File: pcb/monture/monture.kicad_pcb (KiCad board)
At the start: 2 copper layers, 150 x 110 mm, 37 parts, among them U1 Teensy 4.1

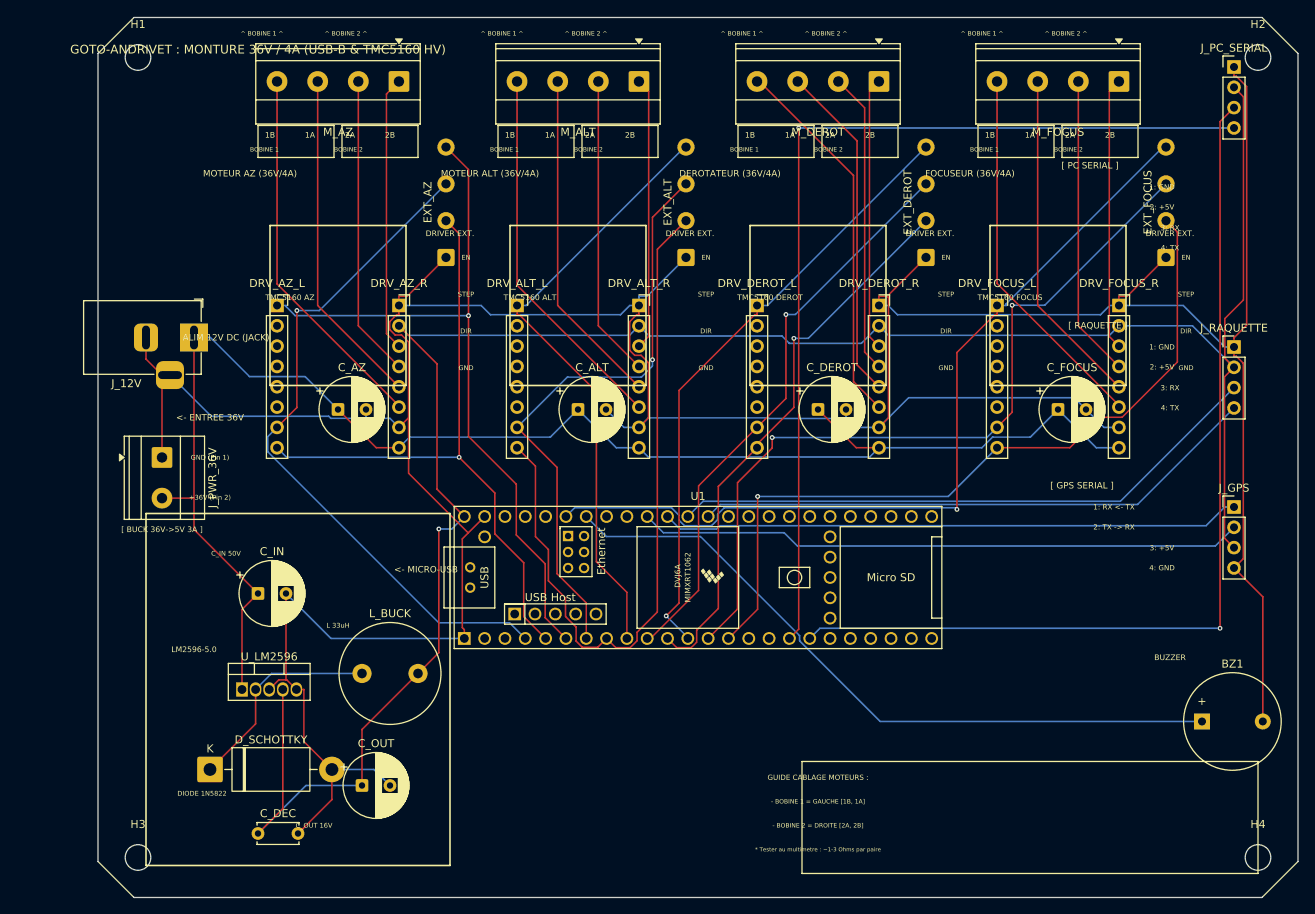
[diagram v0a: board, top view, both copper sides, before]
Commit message: PCB monture : supports StepStick, routage puissance et selecteur de drivers externes
Plan de cablage (README / fiche technique) inchange : memes broches Teensy.

PCB monture
- Supports StepStick a l'entraxe standard 12,7 mm, colonne puissance dans
  l'ordre Pololu (VMOT en face de EN) ; l'ancien brochage mettait le +36V
  sur le +5V via le module. VIO des modules en 3,3 V.
- PC SERIAL : TX6 sur la broche 24 (le PCB cablait la 26), connecteur
  sorti de la zone de vis de H2 (courtyard de H2 restaure).
- Jack 12V isole du bornier 36V par D_JACK (SB560) ; diode du buck SB560
  60V (1N5822 = 40V) ; C_IN 63V deplace hors du passage du cable USB.
- Condensateurs moteur 220uF/63V D10 au-dessus des modules (un 470uF/63V
  D8 n'existe pas et etait sous le module).
- Selecteur par axe StepStick / driver externe : DIP x4 SW_SEL,
  3 x 74HC126 (3,3V) vers les supports, 3 x 74HCT125 (5V) vers les
  pastilles DRIVER EXT. (optocoupleurs M542/DM542).
- Classe de nets "Puissance" 1,5 mm restauree (perdue en f42434d : tout
  etait route en 0,2 mm) ; re-routage Freerouting + finition du buck.
  DRC : 0 erreur, 0 non connecte.
- Serigraphie : etiquettes DRIVER EXT. en face des bons trous, reperes
  EN/VM des supports, conventions RX/TX cote Teensy.

Boitiers
- Monture : ouvertures moteurs recentrees (regression a60715d), trou USB-B
  de nouveau supprime, ouvertures micro-USB Teensy et PC SERIAL, encoche
  du jack ouverte en haut, aerations au-dessus des modules.
- Raquette : trous des boutons centres sur les poussoirs (+3,25 / -2,25).
- Assemblages FreeCAD reconstruits (les App::Part etaient vides) :
  0 interference avec base, couvercle et gabarits.

Firmware Mega : ne plus piloter LED_BUILTIN (= FOCUS_EN broche 13).

build_kicad_pcbs.py aligne sur ces corrections (classes de nets ecrites
dans le .kicad_pro).

Co-Authored-By: Claude Opus 5.5 <noreply@anthropic.com>
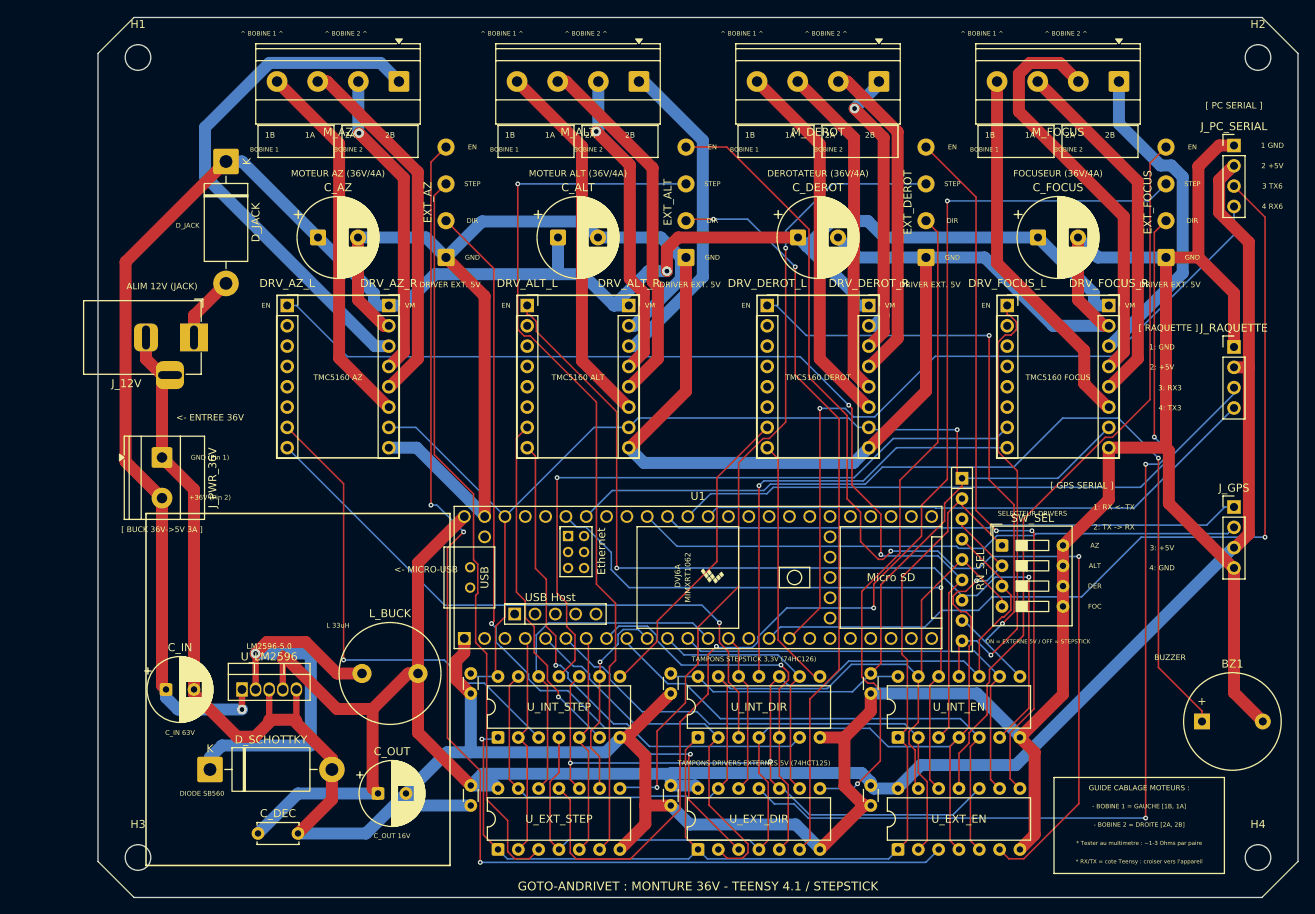
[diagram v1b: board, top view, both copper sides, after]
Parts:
- removed the C_ALT at (60.0, 49.0)
- removed the C_AZ at (30.0, 49.0)
- removed the C_DEROT at (90.0, 49.0)
- removed the C_FOCUS at (120.0, 49.0)
- added C_ALT: 220uF 63V, CP_Radial_D10.0mm_P5.00mm, F.Cu at (57.5, 27.5)
- added C_AZ: 220uF 63V, CP_Radial_D10.0mm_P5.00mm, F.Cu at (27.5, 27.5)
- added C_DEROT: 220uF 63V, CP_Radial_D10.0mm_P5.00mm, F.Cu at (87.5, 27.5)
- added C_EXT_DIR: 100nF, C_Disc_D3.0mm_W1.6mm_P2.50mm, F.Cu at (71.6, 98.5)
- added C_EXT_EN: 100nF, C_Disc_D3.0mm_W1.6mm_P2.50mm, F.Cu at (96.6, 98.5)
- added C_EXT_STEP: 100nF, C_Disc_D3.0mm_W1.6mm_P2.50mm, F.Cu at (46.6, 98.5)
- added C_FOCUS: 220uF 63V, CP_Radial_D10.0mm_P5.00mm, F.Cu at (117.5, 27.5)
- added C_INT_DIR: 100nF, C_Disc_D3.0mm_W1.6mm_P2.50mm, F.Cu at (71.6, 84.5)
- added C_INT_EN: 100nF, C_Disc_D3.0mm_W1.6mm_P2.50mm, F.Cu at (96.6, 84.5)
- added C_INT_STEP: 100nF, C_Disc_D3.0mm_W1.6mm_P2.50mm, F.Cu at (46.6, 84.5)
- added D_JACK: SB560 (60V 5A), D_DO-201AD_P15.24mm_Horizontal, F.Cu at (16.0, 18.0)
- added RN_SEL: 10k x8 (commun broche 1), R_Array_SIP9, F.Cu at (108.0, 57.6)
- added SW_SEL: DIP x4, SW_DIP_SPSTx04_Slide_9.78x12.34mm_W7.62mm_P2.54mm, F.Cu at (113.0, 66.0)
- added U_EXT_DIR: 74HCT125, DIP-14_W7.62mm, F.Cu at (75.0, 104.0)
- added U_EXT_EN: 74HCT125, DIP-14_W7.62mm, F.Cu at (100.0, 104.0)
- added U_EXT_STEP: 74HCT125, DIP-14_W7.62mm, F.Cu at (50.0, 104.0)
- added U_INT_DIR: 74HC126, DIP-14_W7.62mm, F.Cu at (75.0, 90.0)
- added U_INT_EN: 74HC126, DIP-14_W7.62mm, F.Cu at (100.0, 90.0)
- added U_INT_STEP: 74HC126, DIP-14_W7.62mm, F.Cu at (50.0, 90.0)
- C_IN: value 100uF 50V -> 100uF 63V
- D_SCHOTTKY: value 1N5822 (3A) -> SB560 (60V 5A)
- moved C_IN 16.6 mm to (8.50, 84.0)
- moved J_PC_SERIAL 9.81 mm to (142.0, 16.0)
- moved C_OUT 2.24 mm to (35.0, 97.0)
- moved DRV_ALT_R 1.27 mm to (66.3, 36.0)
- moved DRV_DEROT_L 1.27 mm to (83.7, 36.0)
- moved DRV_DEROT_R 1.27 mm to (96.3, 36.0)
- moved DRV_FOCUS_L 1.27 mm to (113.7, 36.0)
- moved DRV_FOCUS_R 1.27 mm to (126.3, 36.0)
- moved DRV_AZ_L 1.27 mm to (23.6, 36.0)
- moved DRV_ALT_L 1.27 mm to (53.6, 36.0)
- moved DRV_AZ_R 1.27 mm to (36.4, 36.0)
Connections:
- DRV_ALT_L pad 1: ALT_EN -> ALT_EN_INT
- DRV_ALT_L pad 7: ALT_STEP -> ALT_STEP_INT
- DRV_ALT_L pad 8: ALT_DIR -> ALT_DIR_INT
- DRV_ALT_R pad 1: GND -> +36V
- DRV_ALT_R pad 2: +5V -> GND
- DRV_ALT_R pad 7: GND -> +3V3
- DRV_ALT_R pad 8: +36V -> GND
- DRV_AZ_L pad 1: AZ_EN -> AZ_EN_INT
- DRV_AZ_L pad 7: AZ_STEP -> AZ_STEP_INT
- DRV_AZ_L pad 8: AZ_DIR -> AZ_DIR_INT
- DRV_AZ_R pad 1: GND -> +36V
- DRV_AZ_R pad 2: +5V -> GND
- DRV_AZ_R pad 7: GND -> +3V3
- DRV_AZ_R pad 8: +36V -> GND
- DRV_DEROT_L pad 1: DEROT_EN -> DEROT_EN_INT
- DRV_DEROT_L pad 7: DEROT_STEP -> DEROT_STEP_INT
- DRV_DEROT_L pad 8: DEROT_DIR -> DEROT_DIR_INT
- DRV_DEROT_R pad 1: GND -> +36V
- DRV_DEROT_R pad 2: +5V -> GND
- DRV_DEROT_R pad 7: GND -> +3V3
- DRV_DEROT_R pad 8: +36V -> GND
- DRV_FOCUS_L pad 1: FOCUS_EN -> FOCUS_EN_INT
- DRV_FOCUS_L pad 7: FOCUS_STEP -> FOCUS_STEP_INT
- DRV_FOCUS_L pad 8: FOCUS_DIR -> FOCUS_DIR_INT
- DRV_FOCUS_R pad 1: GND -> +36V
- DRV_FOCUS_R pad 2: +5V -> GND
- DRV_FOCUS_R pad 7: GND -> +3V3
- DRV_FOCUS_R pad 8: +36V -> GND
- EXT_ALT pad 2: ALT_DIR -> ALT_DIR_EXT
- EXT_ALT pad 3: ALT_STEP -> ALT_STEP_EXT
- EXT_ALT pad 4: ALT_EN -> ALT_EN_EXT
- EXT_AZ pad 2: AZ_DIR -> AZ_DIR_EXT
- EXT_AZ pad 3: AZ_STEP -> AZ_STEP_EXT
- EXT_AZ pad 4: AZ_EN -> AZ_EN_EXT
- EXT_DEROT pad 2: DEROT_DIR -> DEROT_DIR_EXT
- EXT_DEROT pad 3: DEROT_STEP -> DEROT_STEP_EXT
- EXT_DEROT pad 4: DEROT_EN -> DEROT_EN_EXT
- EXT_FOCUS pad 2: FOCUS_DIR -> FOCUS_DIR_EXT
- EXT_FOCUS pad 3: FOCUS_STEP -> FOCUS_STEP_EXT
- EXT_FOCUS pad 4: FOCUS_EN -> FOCUS_EN_EXT
- J_12V pad 1: +36V -> JACK_IN
- U1 pad 16: (no net) -> PC_RX
- U1 pad 18: PC_RX -> (no net)
- U1 pad 46: (no net) -> +3V3
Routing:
- net GND: track 476.6 -> 697.0 mm
- net +3V3: track 0.00 -> 193.0 mm, vias 0 -> 1
- net AZ_EN_EXT: track 0.00 -> 152.8 mm, vias 0 -> 3
- net FOCUS_STEP_EXT: track 0.00 -> 152.6 mm, vias 0 -> 3
- net SEL_AZ: track 0.00 -> 140.6 mm, vias 0 -> 1
- net ALT_EN_EXT: track 0.00 -> 135.7 mm, vias 0 -> 2
- net SEL_ALT: track 0.00 -> 132.9 mm, vias 0 -> 1
- net SEL_DEROT: track 0.00 -> 131.6 mm, vias 0 -> 2
- net FOCUS_DIR_EXT: track 0.00 -> 128.1 mm, vias 0 -> 3
- net AZ_EN_INT: track 0.00 -> 128.1 mm, vias 0 -> 2
- net SEL_FOCUS: track 0.00 -> 123.3 mm
- net ALT_EN_INT: track 0.00 -> 113.7 mm, vias 0 -> 2
- net ALT_STEP_EXT: track 0.00 -> 110.6 mm, vias 0 -> 1
- net DEROT_STEP_EXT: track 0.00 -> 101.4 mm, vias 0 -> 2
- net AZ_DIR_EXT: track 0.00 -> 100.6 mm, vias 0 -> 2
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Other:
- board text added: "* RX/TX = cote Teensy : croiser vers l'appareil"
- board text added: "1 GND"
- board text added: "2 +5V"
- board text added: "3 TX6"
- board text added: "3: RX3"
- board text added: "4 RX6"
- board text added: "4: TX3"
- board text added: "ALIM 12V (JACK)"
- board text added: "ALT"
- board text added: "AZ"
- board text added: "C_IN 63V"
- board text added: "DER"
- board text added: "DIODE SB560"
- board text added: "DRIVER EXT. 5V"
- board text added: "D_JACK"
- board text added: "FOC"
- board text added: "GOTO-ANDRIVET : MONTURE 36V - TEENSY 4.1 / STEPSTICK"
- board text added: "ON = EXTERNE 5V / OFF = STEPSTICK"
- board text added: "SELECTEUR DRIVERS"
- board text added: "TAMPONS DRIVERS EXTERNES 5V (74HCT125)"
- board text added: "TAMPONS STEPSTICK 3,3V (74HC126)"
- board text added: "VM"
- board text removed: "3: RX"
- board text removed: "4: TX"
- board text removed: "ALIM 12V DC (JACK)"
- board text removed: "C_IN 50V"
- board text removed: "DIODE 1N5822"
- board text removed: "DRIVER EXT."
- board text removed: "GOTO-ANDRIVET : MONTURE 36V / 4A (USB-B & TMC5160 HV)"

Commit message: TMC5160 en SPI1 : ponts SPI sur le PCB, configuration par le Teensy
PCB monture :
- 5 ponts a souder par support StepStick (broches 2..6 : SDI, SCK, CSN,
  SDO, CLK) vers le bus SPI1 du Teensy : MOSI 26, SCK 27, MISO 39,
  CS AZ/ALT/DEROT/FOCUS = 41/40/38/37 ; CLK vers GND. Ponts ouverts par
  defaut : A4988, DRV8825, TMC2209 fonctionnent comme avant.
- Re-routage Freerouting : DRC 0 erreur, 0 non connecte, puissance en
  1,5 mm, buck inchange. build_kicad_pcbs.py aligne, rendus regeneres.

Firmware Teensy :
- Detection (IOIN) et configuration des BTT TMC5160 Pro : courant
  (Rsense 0,075), micro-pas, stealthChop ; reconfiguration au retour du
  36V (GSTAT.reset), etat 'E' sur defaut driver, rien pendant un slew.
- Commandes :XTS, :XTI, :XTH, :XTP, :XTM, :XTC ; :XFS lisible.
- Reglages en EEPROM (102-116) ; SPI active au premier demarrage.

Outil de config : section TMC5160 (courants, maintien, stealthChop,
micro-pas DER/FOC, etat par axe), ignoree avec un firmware Mega.

README et fiche technique mis a jour.

Co-Authored-By: Claude Opus 5.5 <noreply@anthropic.com>
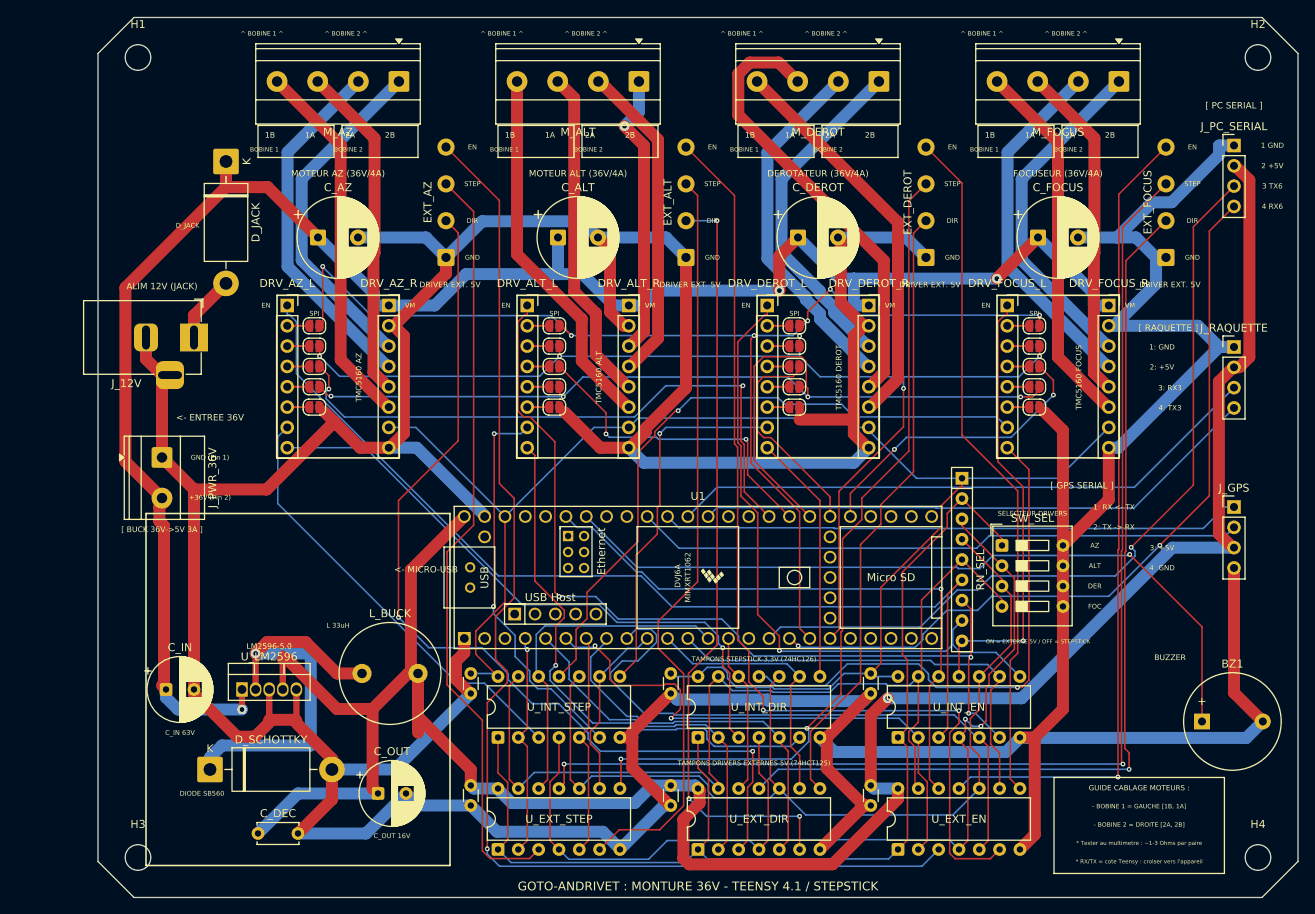
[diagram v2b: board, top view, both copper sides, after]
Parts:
- added JP_ALT_CLK: SPI, SolderJumper-2_P1.3mm_Open_RoundedPad1.0x1.5mm, F.Cu at (57.0, 48.7)
- added JP_ALT_CSN: SPI, SolderJumper-2_P1.3mm_Open_RoundedPad1.0x1.5mm, F.Cu at (57.0, 43.6)
- added JP_ALT_SCK: SPI, SolderJumper-2_P1.3mm_Open_RoundedPad1.0x1.5mm, F.Cu at (57.0, 41.1)
- added JP_ALT_SDI: SPI, SolderJumper-2_P1.3mm_Open_RoundedPad1.0x1.5mm, F.Cu at (57.0, 38.5)
- added JP_ALT_SDO: SPI, SolderJumper-2_P1.3mm_Open_RoundedPad1.0x1.5mm, F.Cu at (57.0, 46.2)
- added JP_AZ_CLK: SPI, SolderJumper-2_P1.3mm_Open_RoundedPad1.0x1.5mm, F.Cu at (27.1, 48.7)
- added JP_AZ_CSN: SPI, SolderJumper-2_P1.3mm_Open_RoundedPad1.0x1.5mm, F.Cu at (27.1, 43.6)
- added JP_AZ_SCK: SPI, SolderJumper-2_P1.3mm_Open_RoundedPad1.0x1.5mm, F.Cu at (27.1, 41.1)
- added JP_AZ_SDI: SPI, SolderJumper-2_P1.3mm_Open_RoundedPad1.0x1.5mm, F.Cu at (27.1, 38.5)
- added JP_AZ_SDO: SPI, SolderJumper-2_P1.3mm_Open_RoundedPad1.0x1.5mm, F.Cu at (27.1, 46.2)
- added JP_DEROT_CLK: SPI, SolderJumper-2_P1.3mm_Open_RoundedPad1.0x1.5mm, F.Cu at (87.0, 48.7)
- added JP_DEROT_CSN: SPI, SolderJumper-2_P1.3mm_Open_RoundedPad1.0x1.5mm, F.Cu at (87.0, 43.6)
- added JP_DEROT_SCK: SPI, SolderJumper-2_P1.3mm_Open_RoundedPad1.0x1.5mm, F.Cu at (87.0, 41.1)
- added JP_DEROT_SDI: SPI, SolderJumper-2_P1.3mm_Open_RoundedPad1.0x1.5mm, F.Cu at (87.0, 38.5)
- added JP_DEROT_SDO: SPI, SolderJumper-2_P1.3mm_Open_RoundedPad1.0x1.5mm, F.Cu at (87.0, 46.2)
- added JP_FOCUS_CLK: SPI, SolderJumper-2_P1.3mm_Open_RoundedPad1.0x1.5mm, F.Cu at (117.0, 48.7)
- added JP_FOCUS_CSN: SPI, SolderJumper-2_P1.3mm_Open_RoundedPad1.0x1.5mm, F.Cu at (117.0, 43.6)
- added JP_FOCUS_SCK: SPI, SolderJumper-2_P1.3mm_Open_RoundedPad1.0x1.5mm, F.Cu at (117.0, 41.1)
- added JP_FOCUS_SDI: SPI, SolderJumper-2_P1.3mm_Open_RoundedPad1.0x1.5mm, F.Cu at (117.0, 38.5)
- added JP_FOCUS_SDO: SPI, SolderJumper-2_P1.3mm_Open_RoundedPad1.0x1.5mm, F.Cu at (117.0, 46.2)
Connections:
- DRV_ALT_L pad 2: (no net) -> ALT_SDI
- DRV_ALT_L pad 3: (no net) -> ALT_SCK
- DRV_ALT_L pad 4: (no net) -> ALT_CSN
- DRV_ALT_L pad 5: (no net) -> ALT_SDO
- DRV_ALT_L pad 6: (no net) -> ALT_CLK
- DRV_AZ_L pad 2: (no net) -> AZ_SDI
- DRV_AZ_L pad 3: (no net) -> AZ_SCK
- DRV_AZ_L pad 4: (no net) -> AZ_CSN
- DRV_AZ_L pad 5: (no net) -> AZ_SDO
- DRV_AZ_L pad 6: (no net) -> AZ_CLK
- DRV_DEROT_L pad 2: (no net) -> DEROT_SDI
- DRV_DEROT_L pad 3: (no net) -> DEROT_SCK
- DRV_DEROT_L pad 4: (no net) -> DEROT_CSN
- DRV_DEROT_L pad 5: (no net) -> DEROT_SDO
- DRV_DEROT_L pad 6: (no net) -> DEROT_CLK
- DRV_FOCUS_L pad 2: (no net) -> FOCUS_SDI
- DRV_FOCUS_L pad 3: (no net) -> FOCUS_SCK
- DRV_FOCUS_L pad 4: (no net) -> FOCUS_CSN
- DRV_FOCUS_L pad 5: (no net) -> FOCUS_SDO
- DRV_FOCUS_L pad 6: (no net) -> FOCUS_CLK
- U1 pad 18: (no net) -> SPI_MOSI
- U1 pad 19: (no net) -> SPI_SCK
- U1 pad 29: (no net) -> SPI_CS_FOCUS
- U1 pad 30: (no net) -> SPI_CS_DEROT
- U1 pad 31: (no net) -> SPI_MISO
- U1 pad 32: (no net) -> SPI_CS_ALT
- U1 pad 33: (no net) -> SPI_CS_AZ
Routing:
- net SPI_MOSI: track 0.00 -> 151.2 mm, vias 0 -> 6
- net SPI_SCK: track 0.00 -> 138.3 mm, vias 0 -> 5
- net SPI_MISO: track 0.00 -> 129.0 mm, vias 0 -> 4
- net SPI_CS_AZ: track 0.00 -> 77.2 mm, vias 0 -> 2
- net SPI_CS_ALT: track 0.00 -> 40.5 mm, vias 0 -> 2
- net SPI_CS_FOCUS: track 0.00 -> 37.6 mm, vias 0 -> 2
- net GND: track 697.0 -> 733.1 mm
- net SPI_CS_DEROT: track 0.00 -> 27.4 mm
- net AZ_2B: track 66.4 -> 42.7 mm
- net +5V: track 263.5 -> 284.7 mm, vias 0 -> 1
- net BUZZER: track 113.9 -> 96.0 mm
- net AZ_DIR_EXT: track 100.6 -> 118.4 mm
- net ALT_STEP_EXT: track 110.6 -> 94.5 mm, vias 1 -> 0
- net DEROT_1A: track 42.0 -> 56.5 mm
- net ALT_EN: track 64.4 -> 77.6 mm
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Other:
- board text added: "SPI"
